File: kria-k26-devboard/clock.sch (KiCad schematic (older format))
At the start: 24 parts, among them U45 SN65LVDS1DR, U46 XLL736027.000000X, Y3 ECS-2520MVLC-260-CM-TR, Y4 AX3DAF1-125.0000

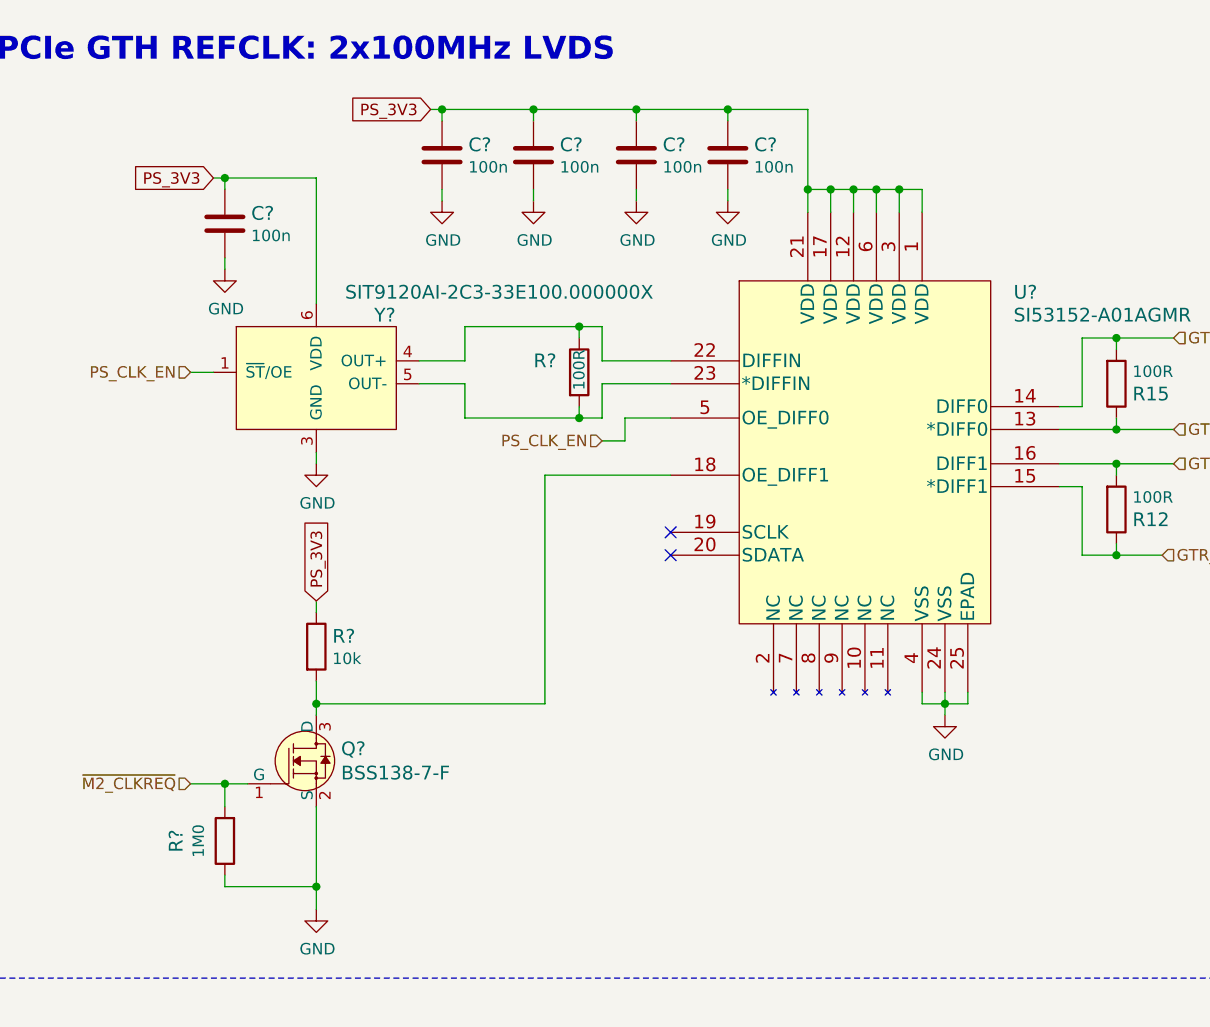
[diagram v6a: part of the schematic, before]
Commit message: Initial placement of power supply
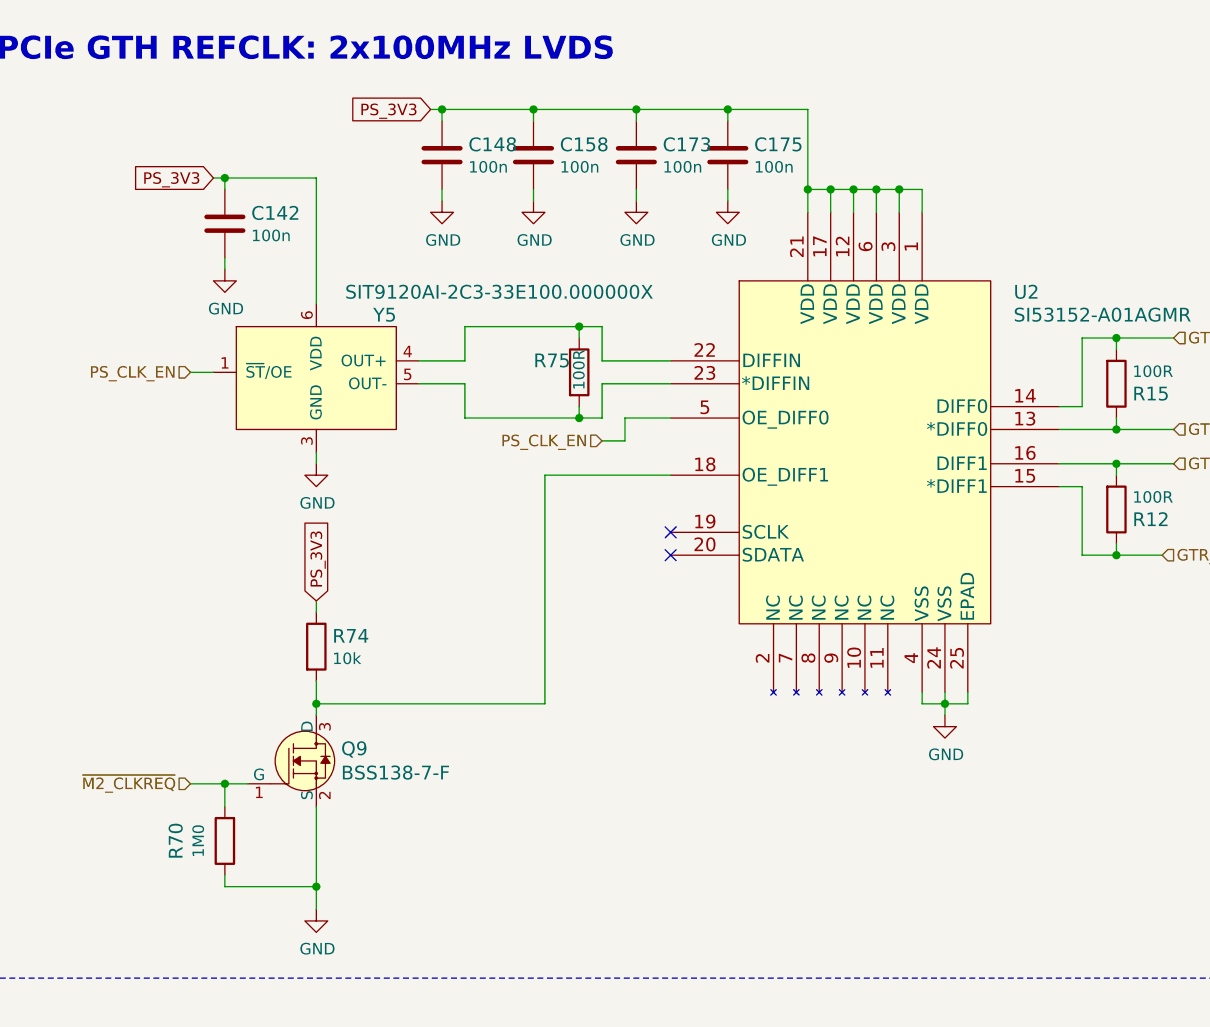
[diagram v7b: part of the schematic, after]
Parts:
- gave numbers to parts that had none: 11
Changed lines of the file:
@@
 	7000 500  7000 6550
 $Comp
-L antmicroOscillators:SIT9120AI-2C3-33E100.000000X Y?
+L antmicroOscillators:SIT9120AI-2C3-33E100.000000X Y5
 U 1 1 6504DD7A
 P 2050 2050
-F 0 "Y?" H 2200 2300 60  0000 C CNN
+F 0 "Y5" H 2200 2300 60  0000 C CNN
 F 1 "SIT9120AI-2C3-33E100.000000X" H 2700 2400 60  0000 C CNN
 F 2 "antmicro-footprints:SiTime_5.0x3.2" H 2250 2250 60  0001 L CNN
@@
 $EndComp
 $Comp
-L antmicroResistors0402:R_100R_0402 R?
+L antmicroResistors0402:R_100R_0402 R75
 U 1 1 65053748
 P 3050 2050
-F 0 "R?" V 3000 1850 60  0000 L CNN
+F 0 "R75" V 3000 1850 60  0000 L CNN
 F 1 "R_100R_0402" H 3050 1900 60  0001 C CNN
 F 2 "antmicro-footprints:0402-res" H 3250 2250 60  0001 L CNN
@@
 	2450 1300 2450 1250
 $Comp
-L power:GND #PWR?
+L power:GND #PWR0278
 U 1 1 65127B75
 P 2450 1300
-F 0 "#PWR?" H 2450 1050 50  0001 C CNN
+F 0 "#PWR0278" H 2450 1050 50  0001 C CNN
 F 1 "GND" H 2455 1127 50  0000 C CNN
 F 2 "" H 2450 1300 50  0001 C CNN
@@
 	2450 950  2450 900
 $Comp
-L antmicroCapacitors0402:C_100n_0402 C?
+L antmicroCapacitors0402:C_100n_0402 C148
 U 1 1 65127B6A
 P 2450 1100
-F 0 "C?" H 2565 1145 60  0000 L CNN
+F 0 "C148" H 2565 1145 60  0000 L CNN
 F 1 "C_100n_0402" H 2450 950 60  0001 C CNN
 F 2 "antmicro-footprints:0402-cap" H 2650 1300 60  0001 L CNN
@@
 	2850 1300 2850 1250
 $Comp
-L power:GND #PWR?
+L power:GND #PWR0281
 U 1 1 65127B5C
 P 2850 1300
-F 0 "#PWR?" H 2850 1050 50  0001 C CNN
+F 0 "#PWR0281" H 2850 1050 50  0001 C CNN
 F 1 "GND" H 2855 1127 50  0000 C CNN
 F 2 "" H 2850 1300 50  0001 C CNN
@@
 	2850 950  2850 900
 $Comp
-L antmicroCapacitors0402:C_100n_0402 C?
+L antmicroCapacitors0402:C_100n_0402 C158
 U 1 1 65127A87
 P 2850 1100
-F 0 "C?" H 2965 1145 60  0000 L CNN
+F 0 "C158" H 2965 1145 60  0000 L CNN
 F 1 "C_100n_0402" H 2850 950 60  0001 C CNN
 F 2 "antmicro-footprints:0402-cap" H 3050 1300 60  0001 L CNN
@@
 	3300 1300 3300 1250
 $Comp
-L power:GND #PWR?
+L power:GND #PWR0303
 U 1 1 650A56D1
 P 3300 1300
-F 0 "#PWR?" H 3300 1050 50  0001 C CNN
+F 0 "#PWR0303" H 3300 1050 50  0001 C CNN
 F 1 "GND" H 3305 1127 50  0000 C CNN
 F 2 "" H 3300 1300 50  0001 C CNN
@@
 	3300 950  3300 900
 $Comp
-L antmicroCapacitors0402:C_100n_0402 C?
+L antmicroCapacitors0402:C_100n_0402 C173
 U 1 1 650A56C6
 P 3300 1100
-F 0 "C?" H 3415 1145 60  0000 L CNN
+F 0 "C173" H 3415 1145 60  0000 L CNN
 F 1 "C_100n_0402" H 3300 950 60  0001 C CNN
 F 2 "antmicro-footprints:0402-cap" H 3500 1300 60  0001 L CNN
@@
 	3700 1300 3700 1250
 $Comp
-L power:GND #PWR?
+L power:GND #PWR0304
 U 1 1 650A56B8
 P 3700 1300
-F 0 "#PWR?" H 3700 1050 50  0001 C CNN
+F 0 "#PWR0304" H 3700 1050 50  0001 C CNN
 F 1 "GND" H 3705 1127 50  0000 C CNN
 F 2 "" H 3700 1300 50  0001 C CNN
@@
 	3700 950  3700 900
 $Comp
-L antmicroCapacitors0402:C_100n_0402 C?
+L antmicroCapacitors0402:C_100n_0402 C175
 U 1 1 650A554F
 P 3700 1100
-F 0 "C?" H 3815 1145 60  0000 L CNN
+F 0 "C175" H 3815 1145 60  0000 L CNN
 F 1 "C_100n_0402" H 3700 950 60  0001 C CNN
 F 2 "antmicro-footprints:0402-cap" H 3900 1300 60  0001 L CNN
@@
 Connection ~ 4050 1250
 $Comp
-L power:GND #PWR?
+L power:GND #PWR0334
 U 1 1 650C9423
 P 4650 3550
-F 0 "#PWR?" H 4650 3300 50  0001 C CNN
+F 0 "#PWR0334" H 4650 3300 50  0001 C CNN
 F 1 "GND" H 4655 3377 50  0000 C CNN
 F 2 "" H 4650 3550 50  0001 C CNN
@@
 $EndComp
 $Comp
-L power:GND #PWR?
+L power:GND #PWR0335
 U 1 1 6517739D
 P 1900 2450
-F 0 "#PWR?" H 1900 2200 50  0001 C CNN
+F 0 "#PWR0335" H 1900 2200 50  0001 C CNN
 F 1 "GND" H 1905 2277 50  0000 C CNN
 F 2 "" H 1900 2450 50  0001 C CNN
@@
 	1500 1600 1500 1550
 $Comp
-L power:GND #PWR?
+L power:GND #PWR0336
 U 1 1 6517F325
 P 1500 1600
-F 0 "#PWR?" H 1500 1350 50  0001 C CNN
+F 0 "#PWR0336" H 1500 1350 50  0001 C CNN
 F 1 "GND" H 1505 1427 50  0000 C CNN
 F 2 "" H 1500 1600 50  0001 C CNN
@@
 	1500 1250 1500 1200
 $Comp
-L antmicroCapacitors0402:C_100n_0402 C?
+L antmicroCapacitors0402:C_100n_0402 C142
 U 1 1 6517F333
 P 1500 1400
-F 0 "C?" H 1615 1445 60  0000 L CNN
+F 0 "C142" H 1615 1445 60  0000 L CNN
 F 1 "C_100n_0402" H 1500 1250 60  0001 C CNN
 F 2 "antmicro-footprints:0402-cap" H 1700 1600 60  0001 L CNN
@@
 P 1900 3750
 AR Path="/65AAF1BF/651A3000" Ref="Q?"  Part="1"
-AR Path="/63C2DC7F/651A3000" Ref="Q?"  Part="1"
-F 0 "Q?" H 2008 3803 60  0000 L CNN
+AR Path="/63C2DC7F/651A3000" Ref="Q9"  Part="1"
+F 0 "Q9" H 2008 3803 60  0000 L CNN
 F 1 "BSS138-7-F" H 2008 3697 60  0000 L CNN
 F 2 "antmicro-footprints:SOT-23-3" H 2100 3950 60  0001 L CNN
@@
 P 1900 4400
 AR Path="/65AAF1BF/651A3008" Ref="#PWR?"  Part="1"
-AR Path="/63C2DC7F/651A3008" Ref="#PWR?"  Part="1"
-F 0 "#PWR?" H 1900 4150 50  0001 C CNN
+AR Path="/63C2DC7F/651A3008" Ref="#PWR0337"  Part="1"
+F 0 "#PWR0337" H 1900 4150 50  0001 C CNN
 F 1 "GND" H 1905 4227 50  0000 C CNN
 F 2 "" H 1900 4400 50  0001 C CNN
@@
 P 1900 3250
 AR Path="/65AAF1BF/651A301F" Ref="R?"  Part="1"
-AR Path="/63C2DC7F/651A301F" Ref="R?"  Part="1"
-F 0 "R?" V 1855 3320 60  0000 L CNN
+AR Path="/63C2DC7F/651A301F" Ref="R74"  Part="1"
+F 0 "R74" V 1855 3320 60  0000 L CNN
 F 1 "R_10k_0402" H 1900 3100 60  0001 C CNN
 F 2 "antmicro-footprints:0402-res" H 2100 3450 60  0001 L CNN
@@
 	1900 3500 2900 3500
 $Comp
-L antmicroResistors0402:R_1M0_0402 R?
+L antmicroResistors0402:R_1M0_0402 R70
 U 1 1 651D6AF3
 P 1500 4100
-F 0 "R?" H 1500 4313 60  0000 C CNN
+F 0 "R70" H 1500 4313 60  0000 C CNN
 F 1 "R_1M0_0402" H 1500 3950 60  0001 C CNN
 F 2 "antmicro-footprints:0402-res" H 1700 4300 60  0001 L CNN
@@
 	8650 5750 8700 5750
 $Comp
-L antmicroLogicBuffersDriversReceiversTransceivers:SI53152-A01AGMR U?
+L antmicroLogicBuffersDriversReceiversTransceivers:SI53152-A01AGMR U2
 U 1 1 6503C5D4
 P 3450 1950
-F 0 "U?" H 4950 2200 60  0000 L CNN
+F 0 "U2" H 4950 2200 60  0000 L CNN
 F 1 "SI53152-A01AGMR" H 4950 2100 60  0000 L CNN
 F 2 "antmicro-footprints:SIL_QFN24_4X4" H 5200 2200 60  0001 C CNN

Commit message: Progress in PCB placement
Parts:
- renumbered C142 to C25, C148 to C26, C158 to C27, C173 to C29, C29 to C30, C175 to C31, C197 to C32, C198 to C33, Q9 to Q3, R70 to R21, R74 to R22, R75 to R23, R16 to R24, R15 to R25, R12 to R26, R98 to R27, R99 to R28, U2 to U6, U45 to U7, U46 to U8, Y5 to Y1, Y3 to Y2, Y4 to Y3
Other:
- moved on the sheet: C25, C26, C27, C28, C29, C30, C31, C32, C33, Q3, R21, R22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
